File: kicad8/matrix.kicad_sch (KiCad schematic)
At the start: 174 parts, among them SW1 ROT_SKYLOONG_HS

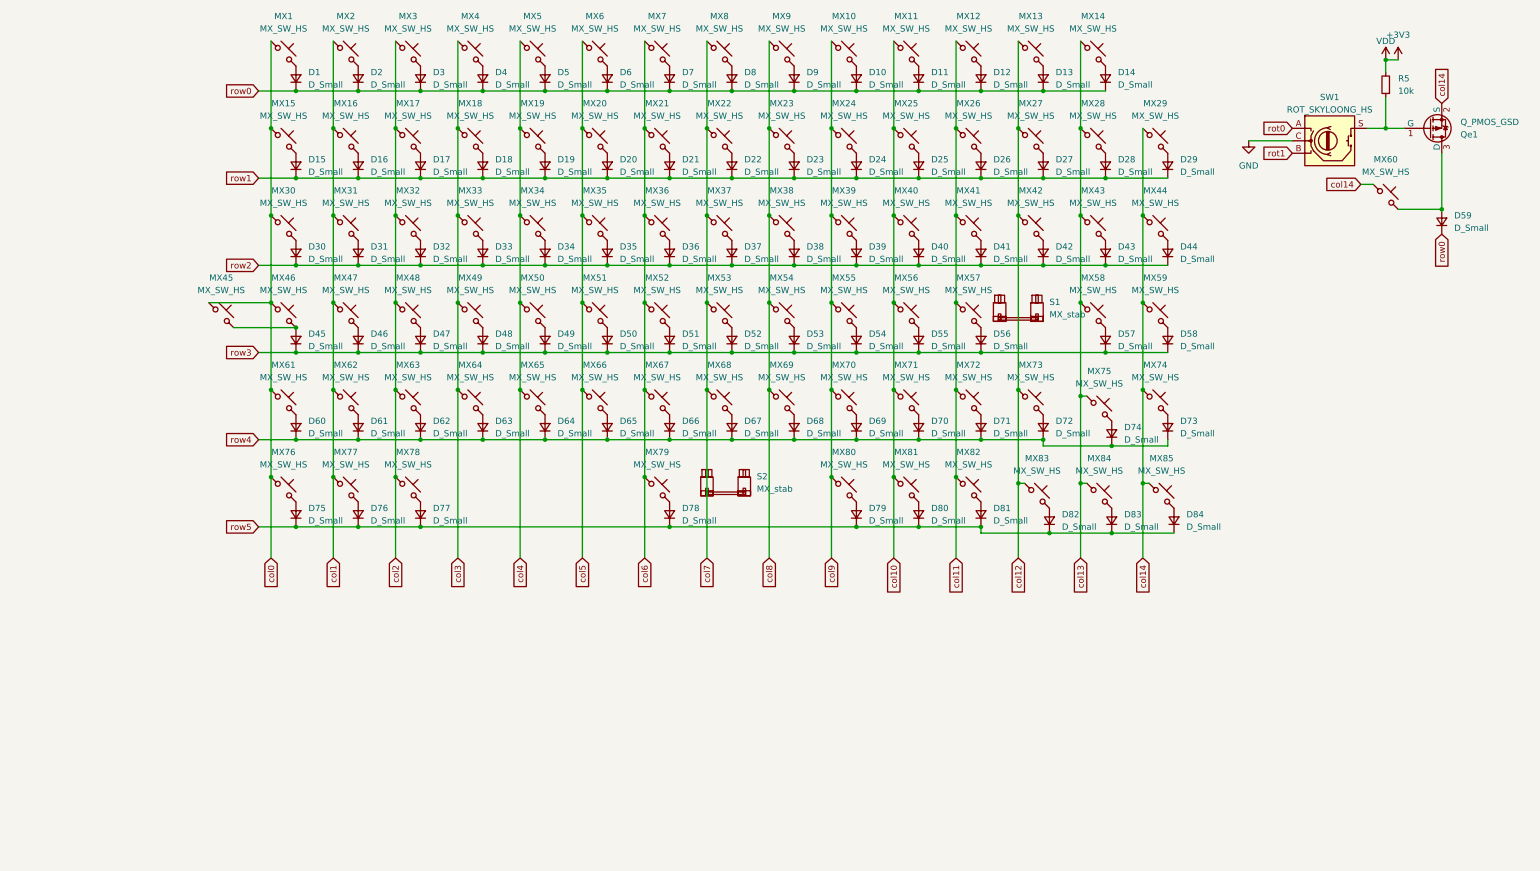
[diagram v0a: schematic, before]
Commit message: Added: more ground fill vias and split space bars
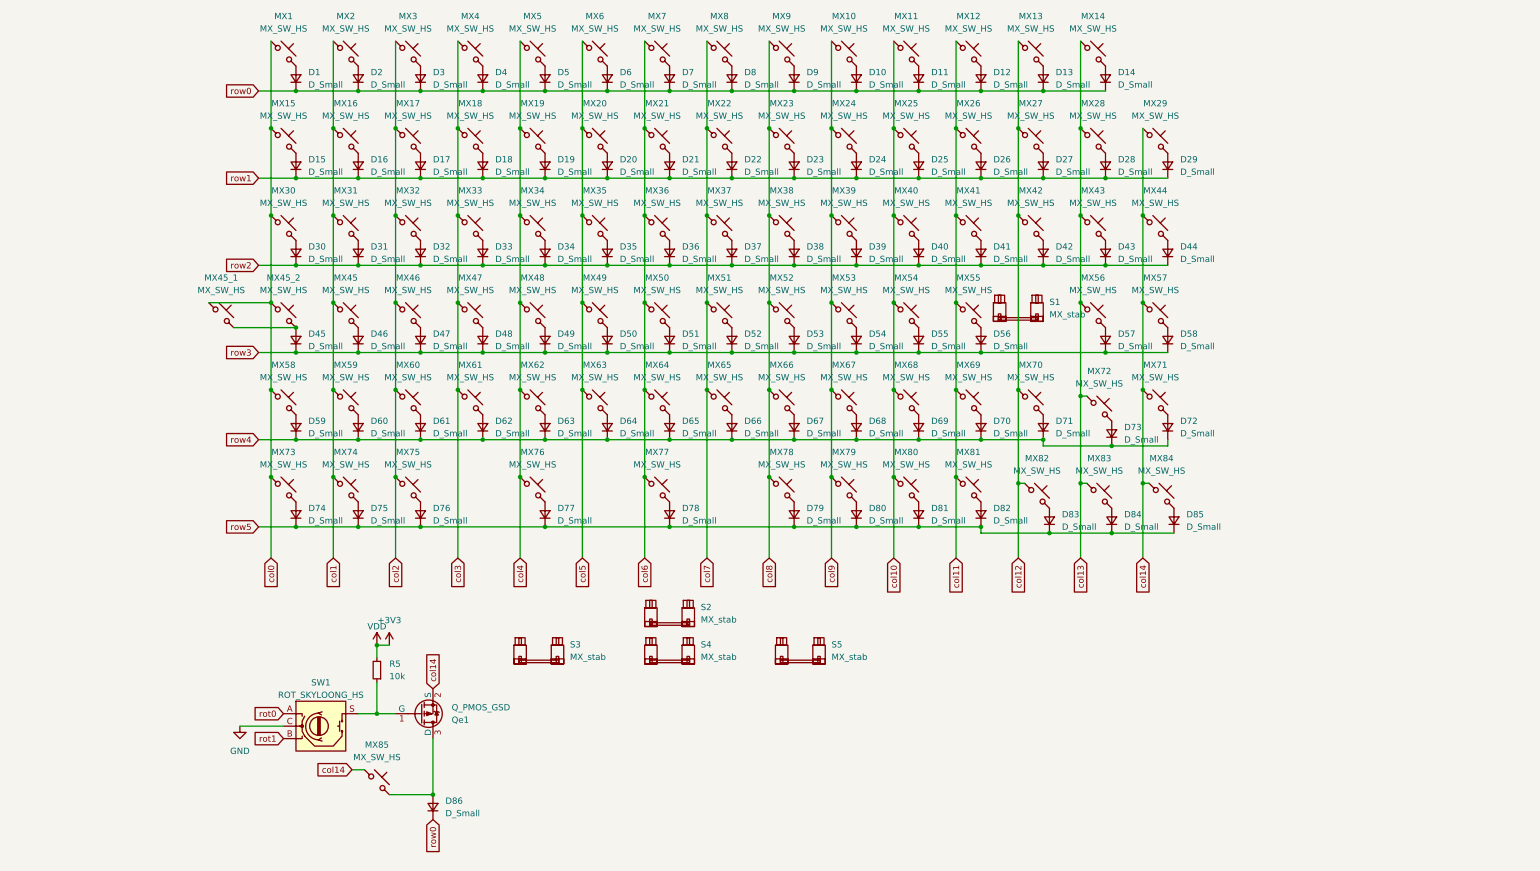
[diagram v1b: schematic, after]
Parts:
- added D77, D79: D_Small, Diode_SMD:D_SOD-123, symbol Device:D_Small
- added MX76, MX78: MX_SW_HS, PCM_marbastlib-mx:SW_MX_HS_CPG151101S11_1u, symbol PCM_marbastlib-mx:MX_SW_HS_CPG151101S11
- added S3, S5: MX_stab, PCM_marbastlib-mx:STAB_MX_P_2u, symbol PCM_marbastlib-mx:MX_stab
- added S4: MX_stab, PCM_marbastlib-mx:STAB_MX_P_2.25u, symbol PCM_marbastlib-mx:MX_stab
- renumbered D60 to D59, D61 to D60, D62 to D61, D63 to D62, D64 to D63, D65 to D64, D66 to D65, D67 to D66, D68 to D67, D69 to D68, D70 to D69, D71 to D70, D72 to D71, D73 to D72, D74 to D73, D75 to D74, D76 to D75, D77 to D76, D79 to D80, D80 to D81, D81 to D82, D82 to D83, D83 to D84, D84 to D85, D59 to D86, MX47 to MX45, MX45 to MX45_1, MX46 to MX45_2, MX48 to MX46, MX49 to MX47, MX50 to MX48, MX51 to MX49, MX52 to MX50, MX53 to MX51, MX54 to MX52, MX55 to MX53, MX56 to MX54, MX57 to MX55, MX58 to MX56, MX59 to MX57, MX61 to MX58, MX62 to MX59, MX63 to MX60, MX64 to MX61, MX65 to MX62, MX66 to MX63, MX67 to MX64, MX68 to MX65, MX69 to MX66, MX70 to MX67, MX71 to MX68, MX72 to MX69, MX73 to MX70, MX74 to MX71, MX75 to MX72, MX76 to MX73, MX77 to MX74, MX78 to MX75, MX79 to MX77, MX80 to MX79, MX81 to MX80, MX82 to MX81, MX83 to MX82, MX84 to MX83, MX85 to MX84, MX60 to MX85
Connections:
- net col4: now also MX76.1
- net col8: now also MX78.1
- net row5: now also D77.1 (K), D79.1 (K)
- new net: D79.2 (A), MX78.2
- new net: D77.2 (A), MX76.2
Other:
- moved on the sheet: D86, MX85, Qe1, R5, S2, SW1

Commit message: Fixed: Silkscreens overlap
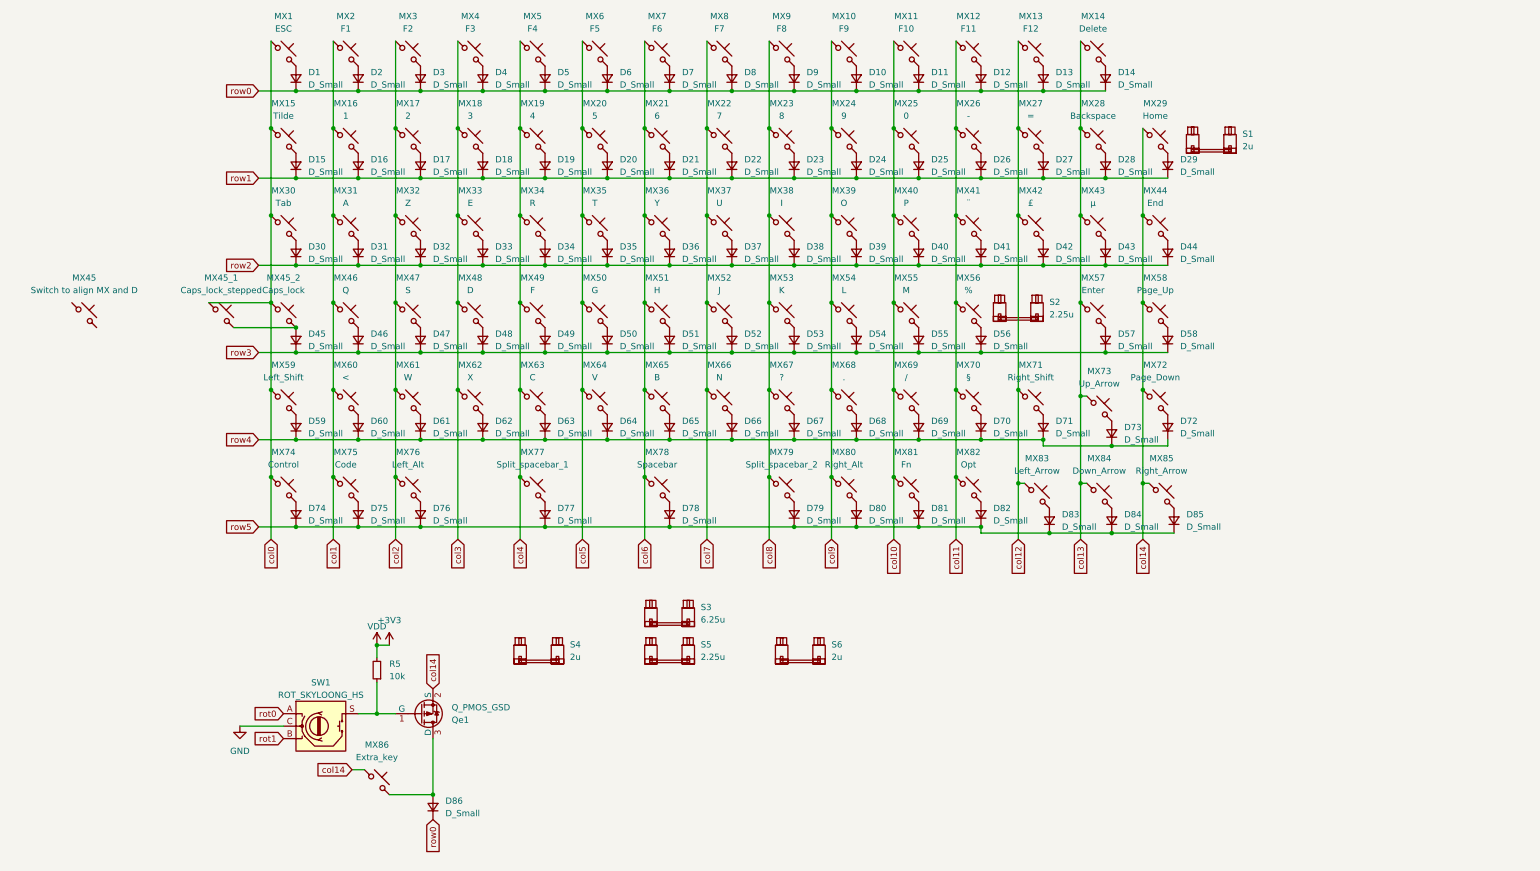
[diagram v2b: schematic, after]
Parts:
- added MX45: Switch to align MX and D, PCM_marbastlib-mx:SW_MX_HS_CPG151101S11_1u, symbol PCM_marbastlib-mx:MX_SW_HS_CPG151101S11
- added S1: 2u, PCM_marbastlib-mx:STAB_MX_P_2u, symbol PCM_marbastlib-mx:MX_stab
- MX1: value MX_SW_HS -> ESC
- MX10: value MX_SW_HS -> F9
- MX11: value MX_SW_HS -> F10
- MX12: value MX_SW_HS -> F11
- MX13: value MX_SW_HS -> F12
- MX14: value MX_SW_HS -> Delete
- MX15: value MX_SW_HS -> Tilde
- MX16: value MX_SW_HS -> 1
- MX17: value MX_SW_HS -> 2
- MX18: value MX_SW_HS -> 3
- MX19: value MX_SW_HS -> 4
- MX2: value MX_SW_HS -> F1
- MX20: value MX_SW_HS -> 5
- MX21: value MX_SW_HS -> 6
- MX22: value MX_SW_HS -> 7
- MX23: value MX_SW_HS -> 8
- MX24: value MX_SW_HS -> 9
- MX25: value MX_SW_HS -> 0
- MX26: value MX_SW_HS -> -
- MX27: value MX_SW_HS -> =
- MX28: value MX_SW_HS -> Backspace
- MX29: value MX_SW_HS -> Home
- MX3: value MX_SW_HS -> F2
- MX30: value MX_SW_HS -> Tab
- MX31: value MX_SW_HS -> A
- MX32: value MX_SW_HS -> Z
- MX33: value MX_SW_HS -> E
- MX34: value MX_SW_HS -> R
- MX35: value MX_SW_HS -> T
- MX36: value MX_SW_HS -> Y
- MX37: value MX_SW_HS -> U
- MX38: value MX_SW_HS -> I
- MX39: value MX_SW_HS -> O
- MX4: value MX_SW_HS -> F3
- MX40: value MX_SW_HS -> P
- MX41: value MX_SW_HS -> ¨
- MX42: value MX_SW_HS -> £
- MX43: value MX_SW_HS -> µ
- MX44: value MX_SW_HS -> End
- MX45_1: value MX_SW_HS -> Caps_lock_stepped
- MX45_2: value MX_SW_HS -> Caps_lock
- MX46: renamed from MX45; value MX_SW_HS -> Q
- MX47: renamed from MX46; value MX_SW_HS -> S
- MX48: renamed from MX47; value MX_SW_HS -> D
- MX49: renamed from MX48; value MX_SW_HS -> F
- MX5: value MX_SW_HS -> F4
- MX50: renamed from MX49; value MX_SW_HS -> G
- MX51: renamed from MX50; value MX_SW_HS -> H
- MX52: renamed from MX51; value MX_SW_HS -> J
- MX53: renamed from MX52; value MX_SW_HS -> K
- MX54: renamed from MX53; value MX_SW_HS -> L
- MX55: renamed from MX54; value MX_SW_HS -> M
- MX56: renamed from MX55; value MX_SW_HS -> %
- MX57: renamed from MX56; value MX_SW_HS -> Enter
- MX58: renamed from MX57; value MX_SW_HS -> Page_Up
- MX59: renamed from MX58; value MX_SW_HS -> Left_Shift
- MX6: value MX_SW_HS -> F5
- MX60: renamed from MX59; value MX_SW_HS -> <
- MX61: renamed from MX60; value MX_SW_HS -> W
- MX62: renamed from MX61; value MX_SW_HS -> X
- MX63: renamed from MX62; value MX_SW_HS -> C
- MX64: renamed from MX63; value MX_SW_HS -> V
- MX65: renamed from MX64; value MX_SW_HS -> B
- MX66: renamed from MX65; value MX_SW_HS -> N
- MX67: renamed from MX66; value MX_SW_HS -> ?
- MX68: renamed from MX67; value MX_SW_HS -> .
- MX69: renamed from MX68; value MX_SW_HS -> /
- MX7: value MX_SW_HS -> F6
- MX70: renamed from MX69; value MX_SW_HS -> §
- MX71: renamed from MX70; value MX_SW_HS -> Right_Shift
- MX72: renamed from MX71; value MX_SW_HS -> Page_Down
- MX73: renamed from MX72; value MX_SW_HS -> Up_Arrow
- MX74: renamed from MX73; value MX_SW_HS -> Control
- MX75: renamed from MX74; value MX_SW_HS -> Code
- MX76: renamed from MX75; value MX_SW_HS -> Left_Alt
- MX77: renamed from MX76; value MX_SW_HS -> Split_spacebar_1
- MX78: renamed from MX77; value MX_SW_HS -> Spacebar
- MX79: renamed from MX78; value MX_SW_HS -> Split_spacebar_2
- MX8: value MX_SW_HS -> F7
- MX80: renamed from MX79; value MX_SW_HS -> Right_Alt
- MX81: renamed from MX80; value MX_SW_HS -> Fn
- MX82: renamed from MX81; value MX_SW_HS -> Opt
- MX83: renamed from MX82; value MX_SW_HS -> Left_Arrow
- MX84: renamed from MX83; value MX_SW_HS -> Down_Arrow
- MX85: renamed from MX84; value MX_SW_HS -> Right_Arrow
- MX86: renamed from MX85; value MX_SW_HS -> Extra_key
- MX9: value MX_SW_HS -> F8
- S2: renamed from S1; value MX_stab -> 2.25u
- S3: renamed from S2; value MX_stab -> 6.25u
- S4: renamed from S3; value MX_stab -> 2u
- S5: renamed from S4; value MX_stab -> 2.25u
- S6: renamed from S5; value MX_stab -> 2u
